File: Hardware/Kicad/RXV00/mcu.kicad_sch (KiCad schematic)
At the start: 32 parts, among them J1 FC, SW1 BOOT, U1 AP2112K-3.3TRG1, U2 ESP32-C3FH4, Y1 40MHz 10pF

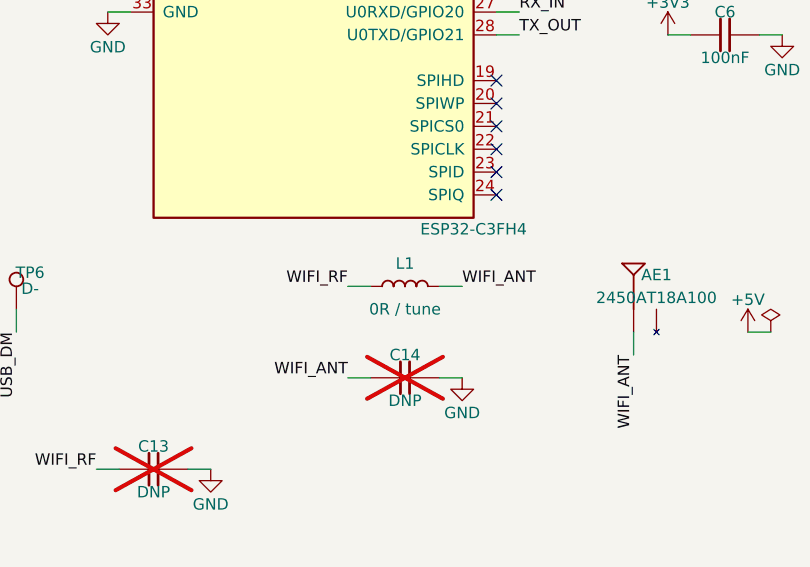
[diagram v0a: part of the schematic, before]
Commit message: Upgrade to KiCad 10 and use shared Kicad_Libs only
- Upgrade ESCV00, FCV00, RXV00, VTXV00 schematics and PCBs to KiCad 10
- Remove KiCad_Libs_Drone and merge_libs (parts already in Kicad_Libs)
- Lib tables list every Kicad_Libs library
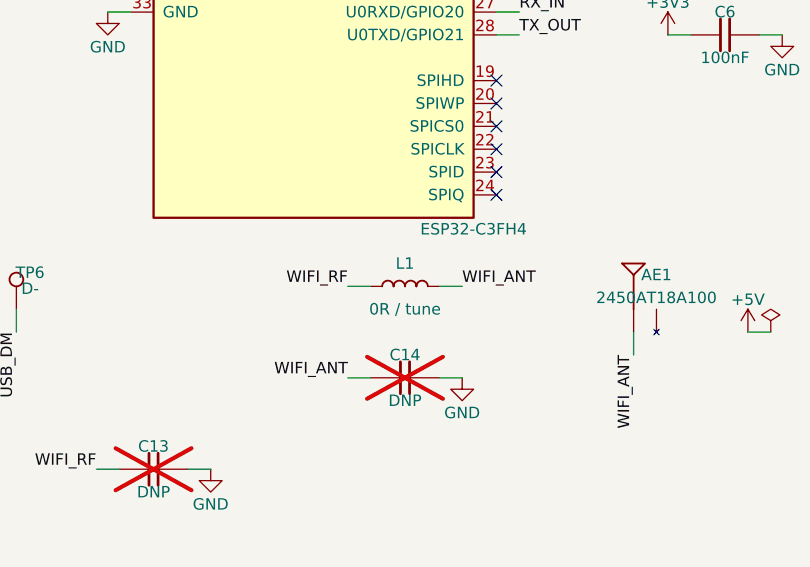
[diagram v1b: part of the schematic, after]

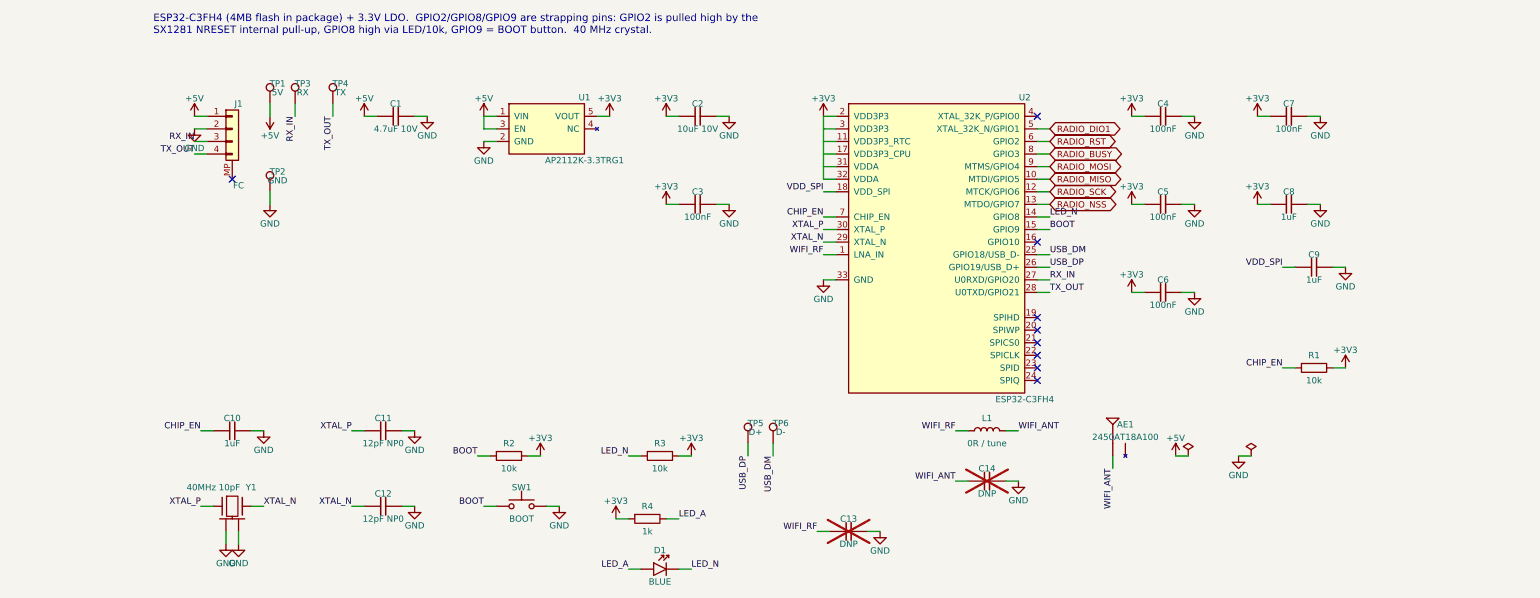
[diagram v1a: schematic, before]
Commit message: Boards follow the B0_EE part convention
- every real part uses the symbol/footprint/3D/datasheet named after its MPN in Kicad_Libs
- symbols keep only Reference, Value, Footprint, Datasheet, Description
  (MPN, Manufacturer, Verify, LCSC, Note fields removed; Verify notes moved to the Readme)
- schematic symbol caches rebuilt from the libraries, PCB footprints relinked with the
  same fields and 3D models as the library (connectivity unchanged)
- DNP and BOM attributes of the footprints match the symbols
- BOMs re-exported with kicad-cli
- ignore KiCad local history
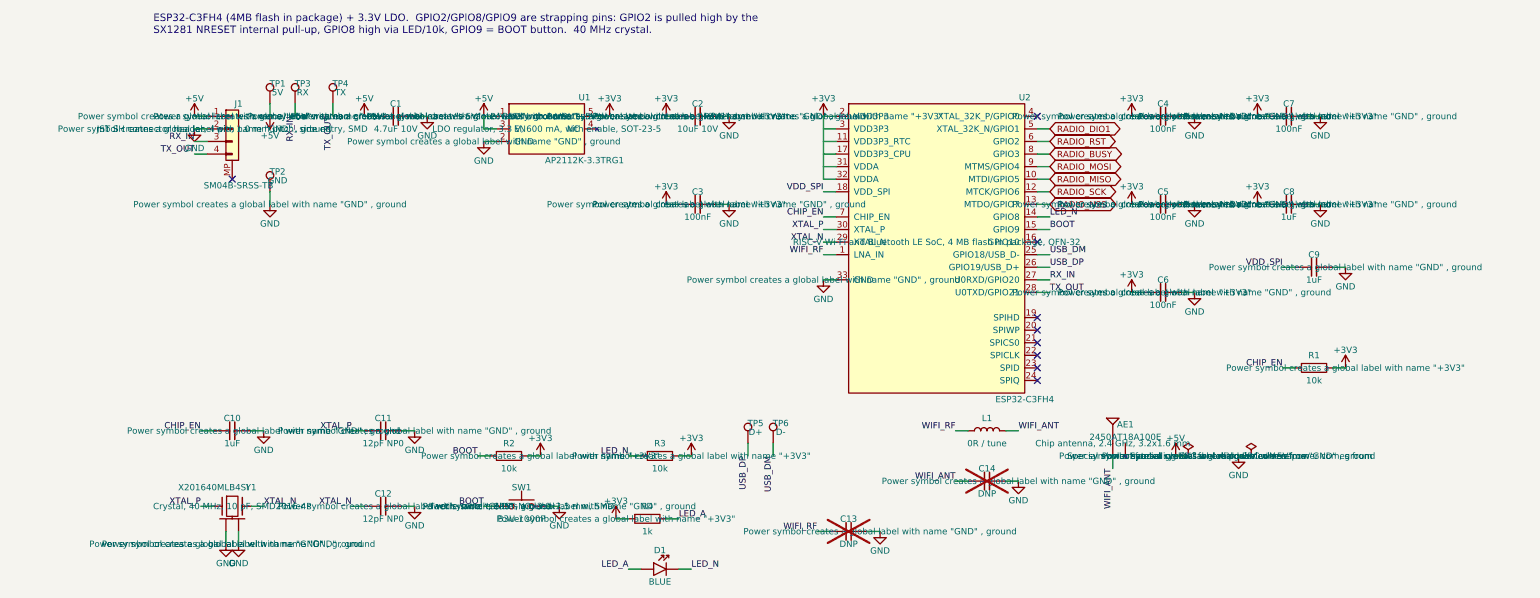
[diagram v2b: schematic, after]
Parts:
- AE1: value 2450AT18A100 -> 2450AT18A100E; footprint eAntenna:Johanson_2450AT18x100 -> eAntenna:2450AT18A100E; symbol eAntenna:Antenna_Chip -> eAntenna:2450AT18A100E; MPN 2450AT18A100E -> (none); Manufacturer Johanson -> (none)
- J1: value FC -> SM04B-SRSS-TB; footprint eConnector:JST_SH_SM04B-SRSS-TB_1x04-1MP_P1.00mm_Horizontal -> eConnector:SM04B-SRSS-TB; symbol eConnector:JST_SH_SM04B-SRSS-TB -> eConnector:SM04B-SRSS-TB; MPN SM04B-SRSS-TB(LF)(SN) -> (none); Manufacturer JST -> (none)
- SW1: value BOOT -> B3U-1000P; footprint eSwitch:SW_SPST_B3U-1000P -> eSwitch:B3U-1000P; symbol eSwitch:SW_Push -> eSwitch:B3U-1000P; MPN B3U-1000P -> (none); Manufacturer Omron -> (none)
- TP1, TP2, TP3, TP4, TP5, TP6: now left out of the parts list
- U1: footprint eLinearReg:SOT-23-5 -> eLinearReg:AP2112K-3.3TRG1; LCSC C51118 -> (none); MPN AP2112K-3.3TRG1 -> (none); Manufacturer Diodes Inc -> (none)
- U2: footprint eMCU:QFN-32-1EP_5x5mm_P0.5mm_EP3.7x3.7mm -> eMCU:ESP32-C3FH4; MPN ESP32-C3FH4 -> (none); Manufacturer Espressif -> (none)
- Y1: value 40MHz 10pF -> X201640MLB4SI; footprint eCrystal:Crystal_SMD_2016-4Pin_2.0x1.6mm -> eCrystal:X201640MLB4SI; symbol eCrystal:Crystal_GND24 -> eCrystal:X201640MLB4SI; MPN X201640MLB4SI -> (none); Manufacturer Yangxing -> (none)

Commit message: Cleared all the descriptions and started Power section for FCV
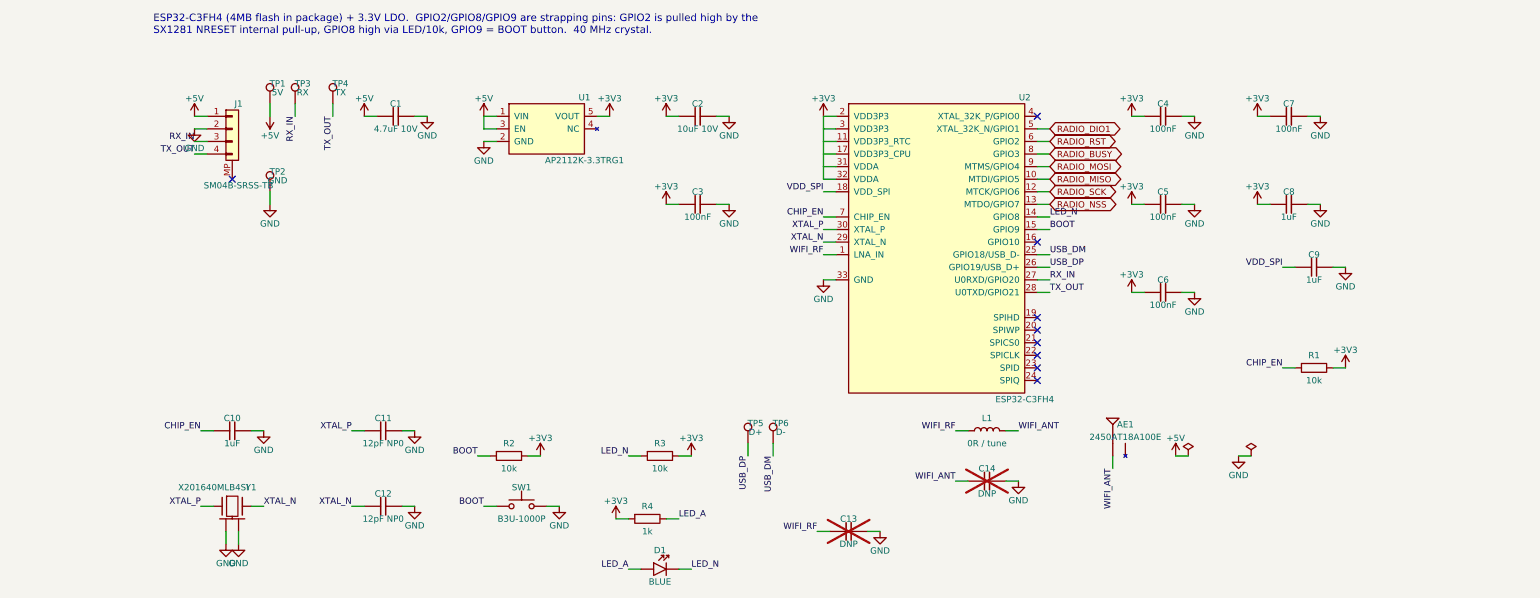
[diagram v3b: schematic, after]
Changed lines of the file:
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@@
 			(show_name no)
 			(do_not_autoplace no)
+			(hide yes)
 			(effects
 				(font
@@
 			(show_name no)
 			(do_not_autoplace no)
+			(hide yes)
 			(effects
 				(font
@@
 			(show_name no)
 			(do_not_autoplace no)
+			(hide yes)
 			(effects
 				(font
@@
 			(show_name no)
 			(do_not_autoplace no)
+			(hide yes)
 			(effects
 				(font
@@
 			(show_name no)
 			(do_not_autoplace no)
+			(hide yes)
 			(effects
 				(font
@@
 			(show_name no)
 			(do_not_autoplace no)
+			(hide yes)
 			(effects
 				(font
@@
 			(show_name no)
 			(do_not_autoplace no)
+			(hide yes)
 			(effects
 				(font
@@
 			(show_name no)
 			(do_not_autoplace no)
+			(hide yes)
 			(effects
 				(font
@@
 			(show_name no)
 			(do_not_autoplace no)
+			(hide yes)
 			(effects
 				(font
@@
 			(show_name no)
 			(do_not_autoplace no)
+			(hide yes)
 			(effects
 				(font
@@
 			(show_name no)
 			(do_not_autoplace no)
+			(hide yes)
 			(effects
 				(font
@@
 			(show_name no)
 			(do_not_autoplace no)
+			(hide yes)
 			(effects
 				(font
@@
 			(show_name no)
 			(do_not_autoplace no)
+			(hide yes)
 			(effects
 				(font
@@
 			(show_name no)
 			(do_not_autoplace no)
+			(hide yes)
 			(effects
 				(font
@@
 			(show_name no)
 			(do_not_autoplace no)
+			(hide yes)
 			(effects
 				(font
@@
 			(show_name no)
 			(do_not_autoplace no)
+			(hide yes)
 			(effects
 				(font
@@
 			(show_name no)
 			(do_not_autoplace no)
+			(hide yes)
 			(effects
 				(font
@@
 			(show_name no)
 			(do_not_autoplace no)
+			(hide yes)
 			(effects
 				(font
@@
 			(show_name no)
 			(do_not_autoplace no)
+			(hide yes)
 			(effects
 				(font
@@
 			(show_name no)
 			(do_not_autoplace no)
+			(hide yes)
 			(effects
 				(font
@@
 			(show_name no)
 			(do_not_autoplace no)
+			(hide yes)
 			(effects
 				(font
@@
 			(show_name no)
 			(do_not_autoplace no)
+			(hide yes)
 			(effects
 				(font
@@
 			(show_name no)
 			(do_not_autoplace no)
+			(hide yes)
 			(effects
 				(font
@@
 			(show_name no)
 			(do_not_autoplace no)
+			(hide yes)
 			(effects
 				(font
@@
 			(show_name no)
 			(do_not_autoplace no)
+			(hide yes)
 			(effects
 				(font
@@
 			(show_name no)
 			(do_not_autoplace no)
+			(hide yes)
 			(effects
 				(font
@@
 			(show_name no)
 			(do_not_autoplace no)
+			(hide yes)
 			(effects
 				(font
@@
 			(show_name no)
 			(do_not_autoplace no)
+			(hide yes)
 			(effects
 				(font
@@
 			(show_name no)
 			(do_not_autoplace no)
+			(hide yes)
 			(effects
 				(font
@@
 			(show_name no)
 			(do_not_autoplace no)
+			(hide yes)
 			(effects
 				(font
@@
 			(show_name no)
 			(do_not_autoplace no)
+			(hide yes)
 			(effects
 				(font
@@
 			(show_name no)
 			(do_not_autoplace no)
+			(hide yes)
 			(effects
 				(font
@@
 			(show_name no)
 			(do_not_autoplace no)
+			(hide yes)
 			(effects
 				(font
@@
 			(show_name no)
 			(do_not_autoplace no)
+			(hide yes)
 			(effects
 				(font
@@
 			(show_name no)
 			(do_not_autoplace no)
+			(hide yes)
 			(effects
 				(font
@@
 			(show_name no)
 			(do_not_autoplace no)
+			(hide yes)
 			(effects
 				(font
@@
 			(show_name no)
 			(do_not_autoplace no)
+			(hide yes)
 			(effects
 				(font
@@
 			(show_name no)
 			(do_not_autoplace no)
+			(hide yes)
 			(effects
 				(font
@@
 			(show_name no)
 			(do_not_autoplace no)
+			(hide yes)
 			(effects
 				(font
@@
 			(show_name no)
 			(do_not_autoplace no)
+			(hide yes)
 			(effects
 				(font
@@
 			(show_name no)
 			(do_not_autoplace no)
+			(hide yes)
 			(effects
 				(font
@@
 			(show_name no)
 			(do_not_autoplace no)
+			(hide yes)
 			(effects
 				(font
@@
 			(show_name no)
 			(do_not_autoplace no)
+			(hide yes)
 			(effects
 				(font
@@
 			(show_name no)
 			(do_not_autoplace no)
+			(hide yes)
 			(effects
 				(font
@@
 			(show_name no)
 			(do_not_autoplace no)
+			(hide yes)
 			(effects
 				(font
@@
 			(show_name no)
 			(do_not_autoplace no)
+			(hide yes)
 			(effects
 				(font
@@
 			(show_name no)
 			(do_not_autoplace no)
+			(hide yes)
 			(effects
 				(font
@@
 			(show_name no)
 			(do_not_autoplace no)
+			(hide yes)
 			(effects
 				(font
